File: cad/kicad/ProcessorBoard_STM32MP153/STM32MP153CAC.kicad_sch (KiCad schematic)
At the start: 45 parts, among them SW201 SW_DIP_x03, U201 STM32MP153CACx, X201 ECS-3225MVQ-240-CN-TR

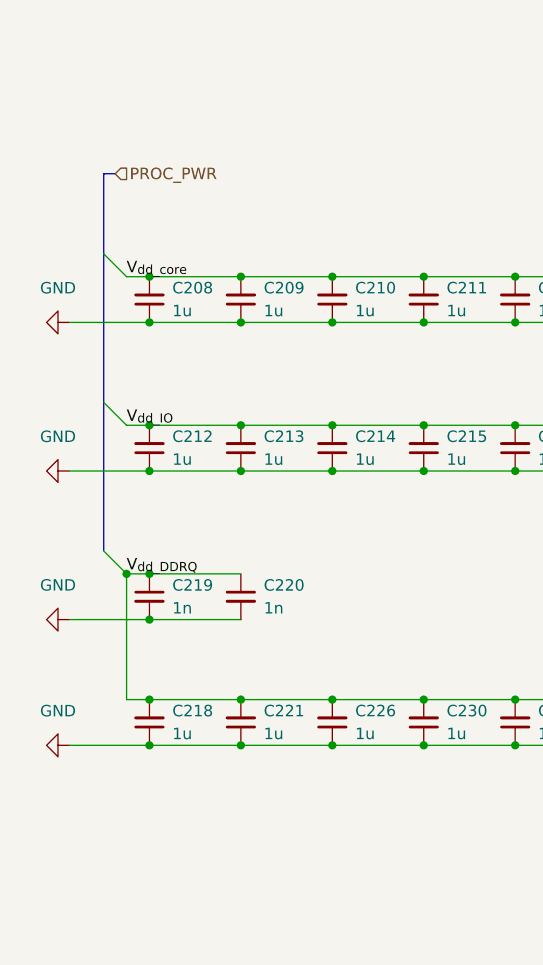
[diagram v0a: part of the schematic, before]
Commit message: realtek bridge thing somewhat more wired
apparently the proper term for via skimping and what not is NFPR (non functional pad removal). all my homies love NFPR. so it is possible to route 0.5mm bga. still fighting the dog but at least cant bring it to another layer
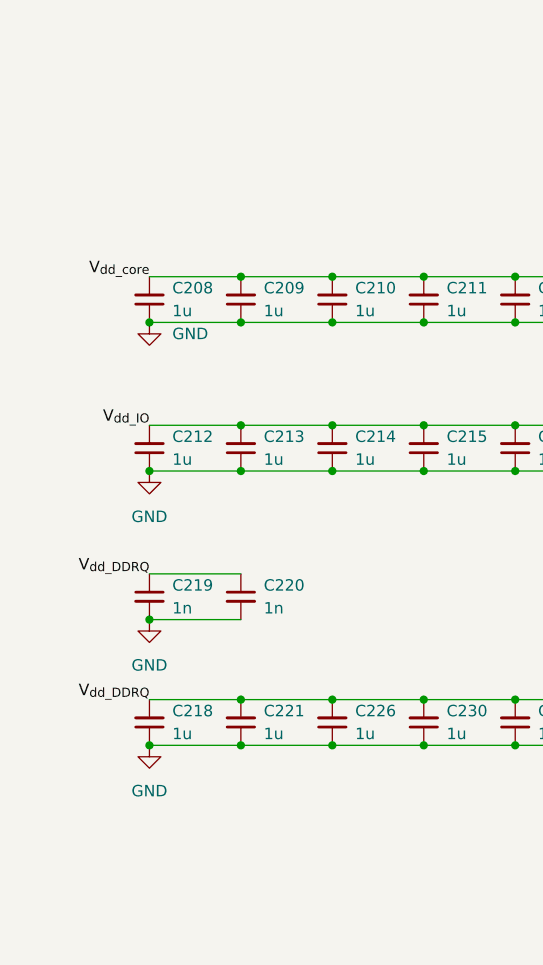
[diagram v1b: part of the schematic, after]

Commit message: miled fixes
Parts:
- C223: value 1u -> 4.7u; footprint Capacitor_SMD:C_0402_1005Metric_Pad0.74x0.62mm_HandSolder -> Capacitor_SMD:C_01005_0402Metric_Pad0.57x0.30mm_HandSolder; character https://ds.murata.com/simsurfing/mlcc.html?partnumbers=%5B%22GRM155R61H105KE05%22%5D&oripartnumbers=%5B%22GRM155R61H105KE05J%22%5D&rgear=suaykx&rgearinfo=com -> https://ds.murata.com/simsurfing/mlcc.html?partnumbers=%5B%22GRM155R60J475ME47%22%5D&oripartnumbers=%5B%22GRM155R60J475ME47J%22%5D&rgear=suaykx&rgearinfo=com; mouser https://www.mouser.com/en/ProductDetail/Murata-Electronics/GRM155R61H105KE05J?qs=d0WKAl%252BL4KZilUxqJ3m7lA%3D%3D -> https://www.mouser.com/en/ProductDetail/Murata-Electronics/GRM155R60J475ME47J?qs=hNud%2FORuBR1o1%2F4Jg%2F%2FSnQ%3D%3D&srsltid=AU7gw4Xa6q2PLsvpnK6qcDhvS62mgMLyQXdMzXB2DHlvS5Pd_XhfAXxY; unit x1 0.11 -> 0.047; unit x10 0.04 -> 0.11
- C229: value 100n -> 1n; footprint Capacitor_SMD:C_0402_1005Metric_Pad0.74x0.62mm_HandSolder -> Capacitor_SMD:C_01005_0402Metric_Pad0.57x0.30mm_HandSolder; character http://ksim.kemet.com/?pn=C0402C104K4PAC7411&disty=mouser -> https://yageogroup.com/products/Capacitors/part/CC0402JRX7R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; mouser https://www.mouser.com/en/ProductDetail/KEMET/C0402C104K4PA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 -> https://www.mouser.com/en/ProductDetail/YAGEO/CC0402JRX7R7B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; unit x10 0.048 -> 0.035
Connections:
- net GND: now also C223.1; no longer C223.2, U201.AB13 (BYPASS_REG1V8)
- net V_{dd_IO}: now also C223.2, C224.2, U201.AB13 (BYPASS_REG1V8), U201.AB14 (VDDA1V8_REG)
- net INTn: now reaches U201.AB3 (PA0)
- net RSTn: now reaches C225.2, U201.M3 (NRST)
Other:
- note removed: "TODO. reset stuff"
- moved on the sheet: C204, C205, C206, C207, C208, C209, C210, C211, C212, C213, C214, C215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

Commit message: all hail the auto router
https://ih1.redbubble.net/image.6083290940.2638/flat,750x,075,f-pad,750x1000,f8f8f8.jpg
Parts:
- C222: value 1u -> 4.7u; character https://ds.murata.com/simsurfing/mlcc.html?partnumbers=%5B%22GRM155R61H105KE05%22%5D&oripartnumbers=%5B%22GRM155R61H105KE05J%22%5D&rgear=suaykx&rgearinfo=com -> https://ds.murata.com/simsurfing/mlcc.html?partnumbers=%5B%22GRM155R60J475ME47%22%5D&oripartnumbers=%5B%22GRM155R60J475ME47J%22%5D&rgear=suaykx&rgearinfo=com; mouser https://www.mouser.com/en/ProductDetail/Murata-Electronics/GRM155R61H105KE05J?qs=d0WKAl%252BL4KZilUxqJ3m7lA%3D%3D -> https://www.mouser.com/en/ProductDetail/Murata-Electronics/GRM155R60J475ME47J?qs=hNud%2FORuBR1o1%2F4Jg%2F%2FSnQ%3D%3D&srsltid=AU7gw4Xa6q2PLsvpnK6qcDhvS62mgMLyQXdMzXB2DHlvS5Pd_XhfAXxY; unit x1 0.11 -> 0.047; unit x10 0.04 -> 0.11
- C223, C229: footprint Capacitor_SMD:C_01005_0402Metric_Pad0.57x0.30mm_HandSolder -> Capacitor_SMD:C_0402_1005Metric_Pad0.74x0.62mm_HandSolder
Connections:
- net GND: now also C222.1; no longer C222.2
- net at U201.AB15 (VDDA1V1_REG): now also C222.2; no longer C222.1
- net CASn renamed ddr.CASn
- net CKE renamed ddr.CKE
- net CLK_N renamed ddr.CLK_N
- net CLK_P renamed ddr.CLK_P
- net CSn renamed ddr.CSn
- net ODT renamed ddr.ODT
- net RASn renamed ddr.RASn
- net RESETn renamed ddr.RESETn
- net WEN renamed ddr.WEN
- net a0 renamed ddr.a0
- net a1 renamed ddr.a1
- net a2 renamed ddr.a2
- net a3 renamed ddr.a3
- net a4 renamed ddr.a4
- net a5 renamed ddr.a5
- net a6 renamed ddr.a6
- net a7 renamed ddr.a7
- net a8 renamed ddr.a8
- net a9 renamed ddr.a9
- net b0 renamed ddr.b0
- net b1 renamed ddr.b1
- net b2 renamed ddr.b2
- net d0 renamed ddr.d0
- net d1 renamed ddr.d1
- net d10 renamed ddr.d10
- net d11 renamed ddr.d11
- net d12 renamed ddr.d12
- net d13 renamed ddr.d13
- net d14 renamed ddr.d14
- net d15 renamed ddr.d15
- net d16 renamed ddr.d16
- net d17 renamed ddr.d17
- net d18 renamed ddr.d18
- net d19 renamed ddr.d19
- net d2 renamed ddr.d2
- net d20 renamed ddr.d20
- net d21 renamed ddr.d21
- net d22 renamed ddr.d22
- net d23 renamed ddr.d23
- net d24 renamed ddr.d24
- net d25 renamed ddr.d25
- net d26 renamed ddr.d26
- net d27 renamed ddr.d27
- net d28 renamed ddr.d28
- net d29 renamed ddr.d29
- net d3 renamed ddr.d3
- net d30 renamed ddr.d30
- net d31 renamed ddr.d31
- net d4 renamed ddr.d4
- net d5 renamed ddr.d5
- net d6 renamed ddr.d6
- net d7 renamed ddr.d7
- net d8 renamed ddr.d8
- net d9 renamed ddr.d9
- net m0 renamed ddr.m0
- net m1 renamed ddr.m1
- net m2 renamed ddr.m2
- net m3 renamed ddr.m3
- net s0_N renamed ddr.s0_N
- net s0_P renamed ddr.s0_P
- net s1_N renamed ddr.s1_N
- net s1_P renamed ddr.s1_P
- net s2_N renamed ddr.s2_N
- net s2_P renamed ddr.s2_P
- net s3_N renamed ddr.s3_N
- net s3_P renamed ddr.s3_P

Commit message: somewhat fanned
the auto router sucks :( . and the auto fanout sucks. and i routed everything on the wrong grid and it snapped to teh wrong places and i only noticed most of teh way though so i push and make it tomorrows problem
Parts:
- renumbered C208 to C201, C212 to C202, C219 to C203, C218 to C204, C209 to C205, C213 to C206, C220 to C207, C221 to C208, C210 to C209, C214 to C210, C226 to C211, C211 to C212, C215 to C213, C230 to C214, C207 to C215, C231 to C217, C206 to C218, C217 to C219, C232 to C220, C205 to C221, C233 to C222, C204 to C223, C227 to C224, C203 to C225, C225 to C226, C229 to C227, C201 to C228, C202 to C229, C222 to C230, C223 to C231, C224 to C232, C228 to C233, R205 to R201, R206 to R202, R207 to R203, R208 to R204, R201 to R205, R202 to R206, R203 to R207, R204 to R208

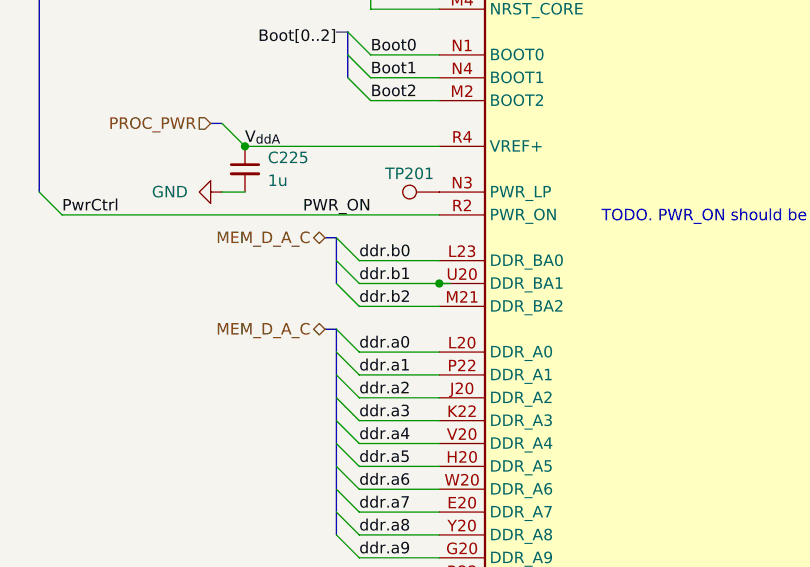
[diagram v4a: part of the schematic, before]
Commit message: where ram :(
its 56 connecitons (not including pwr and gnd) for x32 bus. not possible witout HDI or increasing layer count, both are big bucks. so long china ram. apparently winabond has some hidden gems and ebay smugglers as a supply chain. good stuff. and micron gatekeeps theyre datasheets.
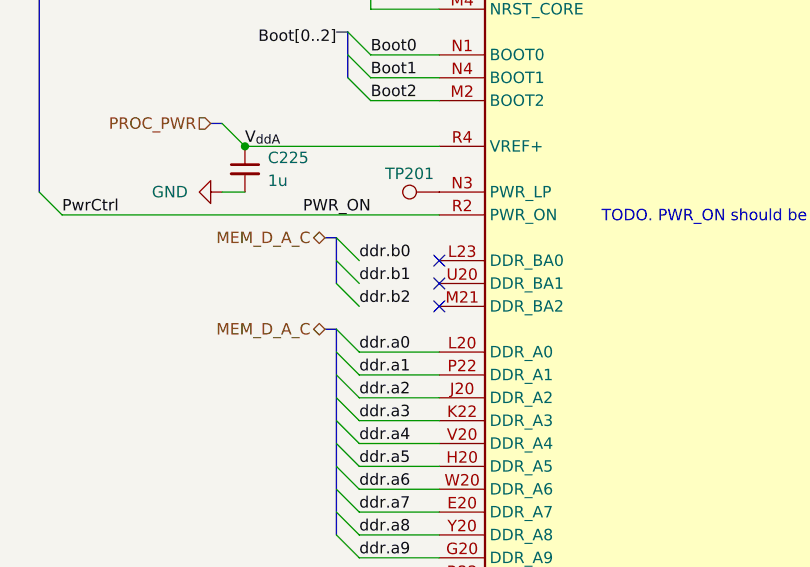
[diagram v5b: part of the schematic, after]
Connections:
- net ddr.b0: no longer U201.L23 (DDR_BA0)
- net ddr.b1: no longer U201.U20 (DDR_BA1)
- net ddr.b2: no longer U201.M21 (DDR_BA2)
- no-connect marks 17 -> 20
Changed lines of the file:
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@@
-	)
-	(junction
-		(at 172.72 80.01)
-		(diameter 0)
-		(color 0 0 0 0)
 	)
 	(junction
@@
 	)
 	(no_connect
+		(at 172.72 82.55)
+	)
+	(no_connect
 		(at 172.72 125.73)
 	)
@@
 	)
 	(no_connect
+		(at 172.72 77.47)
+	)
+	(no_connect
 		(at 172.72 123.19)
 	)
@@
 		(at 172.72 293.37)
 	)
+	(no_connect
+		(at 172.72 80.01)
+	)
 	(bus_entry
 		(at 161.29 102.87)
@@
 	(wire
 		(pts
-			(xy 163.83 82.55) (xy 172.72 82.55)
-		)
-		(stroke
-			(width 0)
-			(type default)
-		)
-	)
-	(wire
-		(pts
 			(xy 67.31 166.37) (xy 77.47 166.37)
 		)
@@
 	(wire
 		(pts
-			(xy 173.99 80.01) (xy 172.72 80.01)
-		)
-		(stroke
-			(width 0)
-			(type default)
-		)
-	)
-	(wire
-		(pts
 			(xy 233.68 29.21) (xy 233.68 36.83)
 		)
@@
 	(wire
 		(pts
-			(xy 163.83 77.47) (xy 172.72 77.47)
-		)
-		(stroke
-			(width 0)
-			(type default)
-		)
-	)
-	(wire
-		(pts
 			(xy 163.83 135.89) (xy 172.72 135.89)
 		)
@@
 		)
 		(stroke
-			(width 0)
-			(type default)
-		)
-	)
-	(wire
-		(pts
-			(xy 163.83 80.01) (xy 172.72 80.01)
-		)
-		(stroke

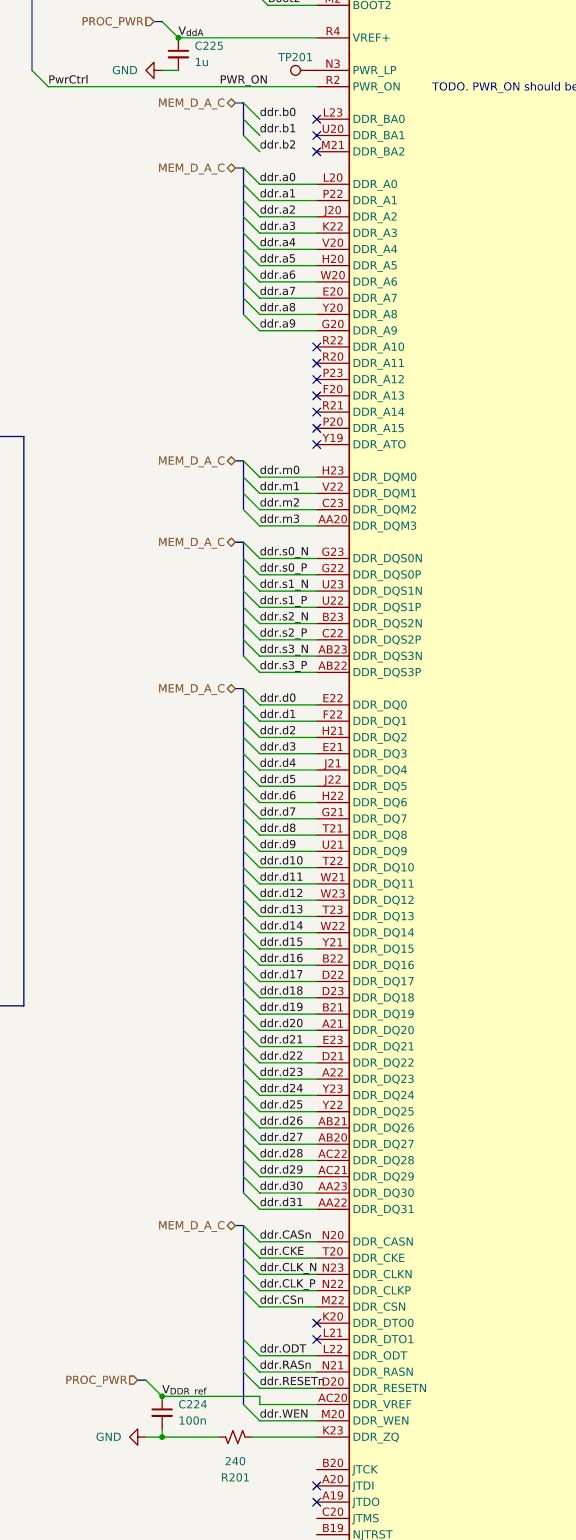
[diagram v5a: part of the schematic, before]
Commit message: 2 layer ddr route. un tuned, missing pwr
initial ddr rout done, not lenght tuned, only impedance matched. layer 1 completely free of traces, need to put power planes on it
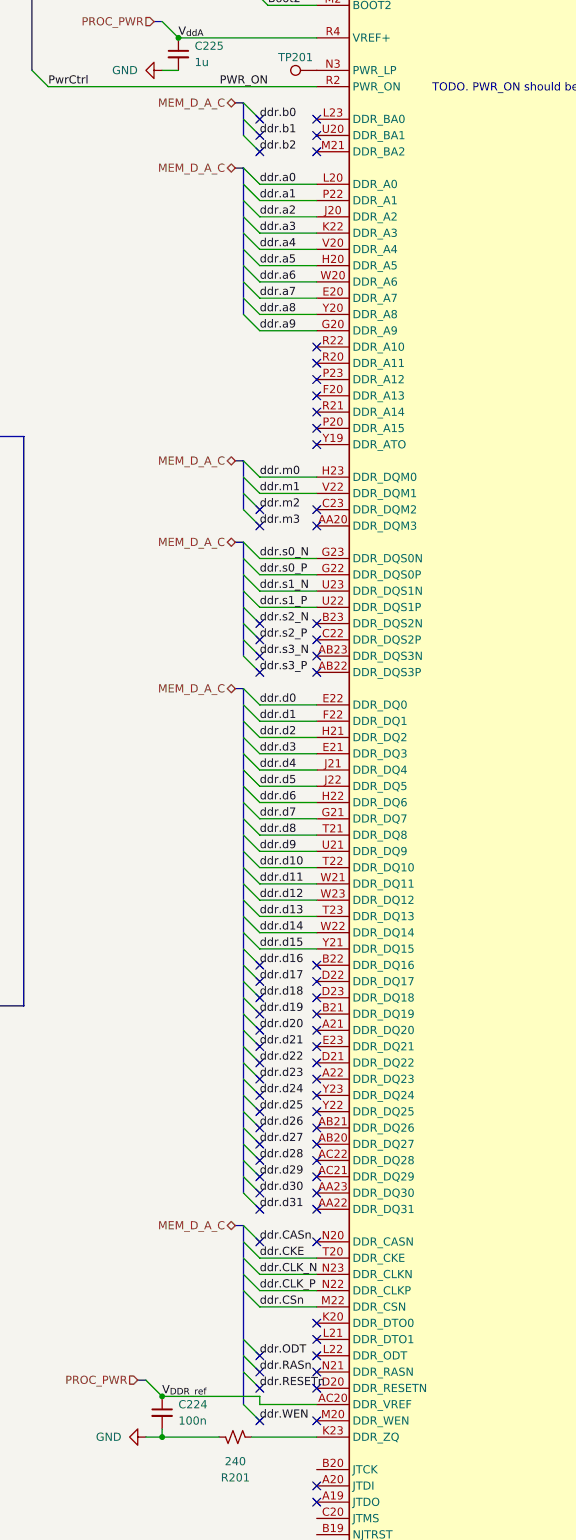
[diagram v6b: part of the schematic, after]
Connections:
- net ddr.CASn: no longer U201.N20 (DDR_CASN)
- net ddr.ODT: no longer U201.L22 (DDR_ODT)
- net ddr.RASn: no longer U201.N21 (DDR_RASN)
- net ddr.RESETn: no longer U201.D20 (DDR_RESETN)
- net ddr.WEN: no longer U201.M20 (DDR_WEN)
- net ddr.d16: no longer U201.B22 (DDR_DQ16)
- net ddr.d17: no longer U201.D22 (DDR_DQ17)
- net ddr.d18: no longer U201.D23 (DDR_DQ18)
- net ddr.d19: no longer U201.B21 (DDR_DQ19)
- net ddr.d20: no longer U201.A21 (DDR_DQ20)
- net ddr.d21: no longer U201.E23 (DDR_DQ21)
- net ddr.d22: no longer U201.D21 (DDR_DQ22)
- net ddr.d23: no longer U201.A22 (DDR_DQ23)
- net ddr.d24: no longer U201.Y23 (DDR_DQ24)
- net ddr.d25: no longer U201.Y22 (DDR_DQ25)
- net ddr.d26: no longer U201.AB21 (DDR_DQ26)
- net ddr.d27: no longer U201.AB20 (DDR_DQ27)
- net ddr.d28: no longer U201.AC22 (DDR_DQ28)
- net ddr.d29: no longer U201.AC21 (DDR_DQ29)
- net ddr.d30: no longer U201.AA23 (DDR_DQ30)
- net ddr.d31: no longer U201.AA22 (DDR_DQ31)
- net ddr.m2: no longer U201.C23 (DDR_DQM2)
- net ddr.m3: no longer U201.AA20 (DDR_DQM3)
- net ddr.s2_N: no longer U201.B23 (DDR_DQS2N)
- net ddr.s2_P: no longer U201.C22 (DDR_DQS2P)
- net ddr.s3_N: no longer U201.AB23 (DDR_DQS3N)
- net ddr.s3_P: no longer U201.AB22 (DDR_DQS3P)
- no-connect marks 20 -> 77

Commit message: boo womp 10000
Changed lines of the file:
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@@
+		)
+	)
+	(label "sfp{rgmii sfp_io}"
+		(at 533.4 245.11 180)
+		(effects
+			(font
+				(size 1.27 1.27)
+			)
+			(justify right)
 		)
 	)
@@
 		)
 	)
+	(hierarchical_label "SFP_BRIDGE"
+		(shape bidirectional)
+		(at 533.4 245.11 0)
+		(effects
+			(font
+				(size 1.27 1.27)
+			)
+			(justify left)
+		)
+	)

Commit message: found reference schematic :he he he ha:
coincidence using the same chip !? am i tweaking or tamale-n brap
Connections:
- net sfp.txd1: now reaches U201.AA1 (PG14)
- net sfp.txd0: now reaches U201.AA2 (PG13)
- net sfp.rxc: now reaches U201.AA4 (PA1)
- net sfp.mdc: now reaches U201.AA6 (PC1)
- net sfp.txc: now reaches U201.AB2 (PG4)
- net sfp.rxd1: now reaches U201.AB7 (PC5)
- net sfp.rxctl: now reaches U201.AB8 (PA7)
- net sfp.mdio: now reaches U201.AC3 (PA2)
- net sfp.rxd0: now reaches U201.AC7 (PC4)
- net sfp.phy.int#: now reaches U201.K4 (PG12)
- net sfp.rxd3: now reaches U201.W4 (PH7)
- net sfp.txd3: now reaches U201.Y1 (PE2)
- net sfp.rxd2: now reaches U201.Y11 (PH6)
- net sfp.txd2: now reaches U201.Y2 (PC2)
- net sfp.phymac_frclk_125: now reaches U201.Y6 (PG5)
- net sfp.txctl: now reaches U201.Y7 (PG11)
- net sfp.macphy_clk_25: now reaches U201.Y8 (PB5)
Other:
- moved on the sheet: C201, C202, C203, C204, C205, C206, C207, C208, C209, C210, C211, C212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
